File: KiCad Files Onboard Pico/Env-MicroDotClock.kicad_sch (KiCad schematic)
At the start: 59 parts, among them IC1 IS31FL3730-QFLS2-TR, IC2 IS31FL3730-QFLS2-TR, IC3 IS31FL3730-QFLS2-TR, IC4 IS31FL3730-QFLS2-TR, J1 Conn_01x06_Pin, M1 Dip-14 Socket, M2 Dip-14 Socket, M3 Dip-14 Socket, M4 Dip-14 Socket, M5 Dip-14 Socket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

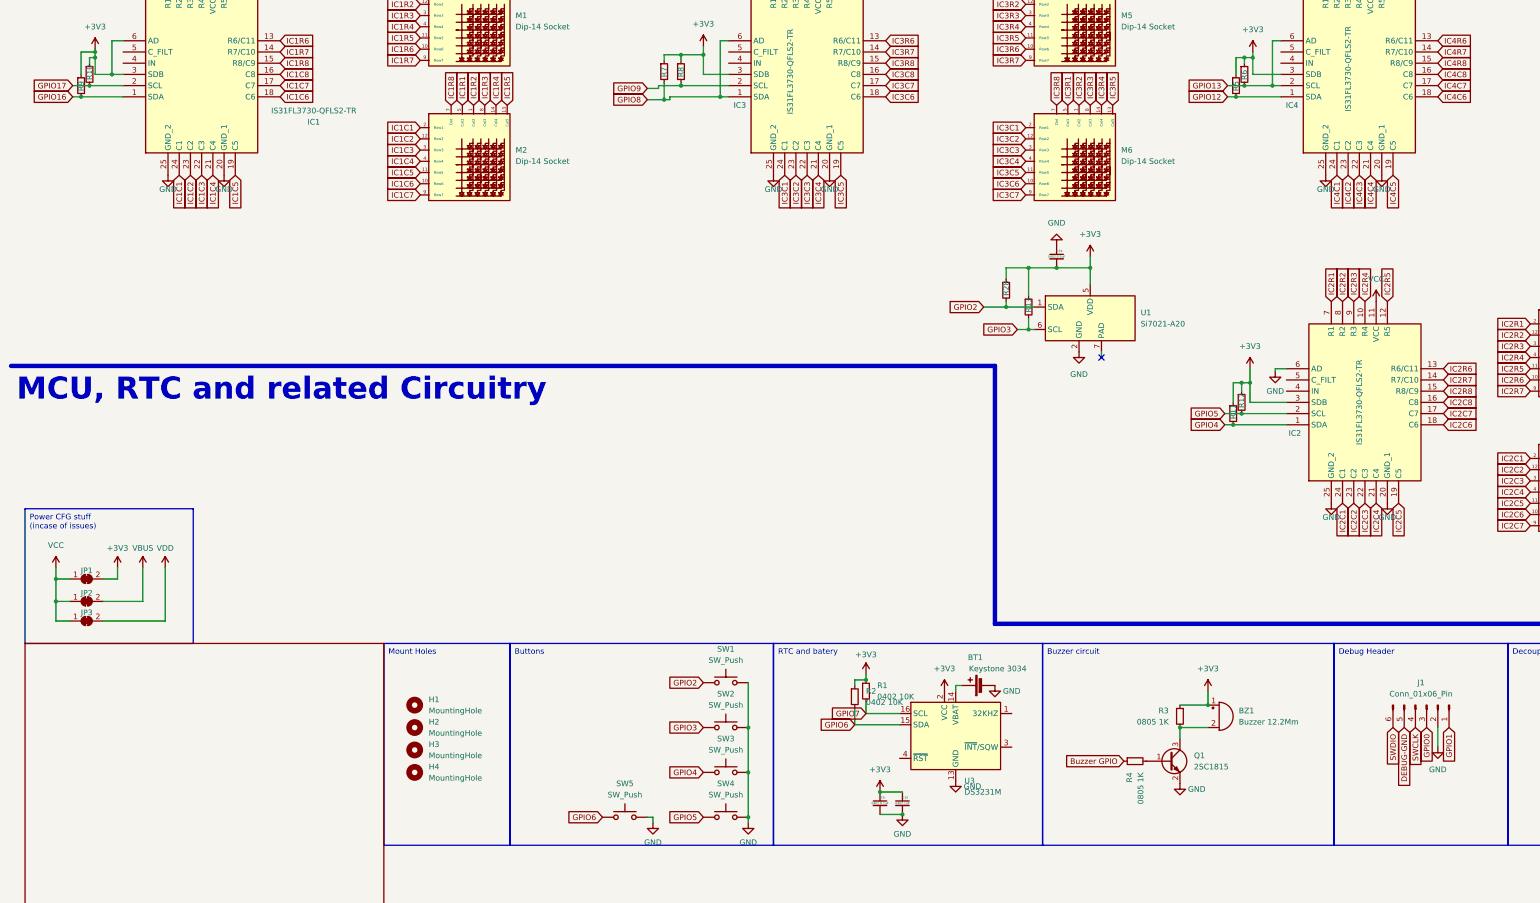
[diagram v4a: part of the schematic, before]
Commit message: began rework of onboard 2040 pcb
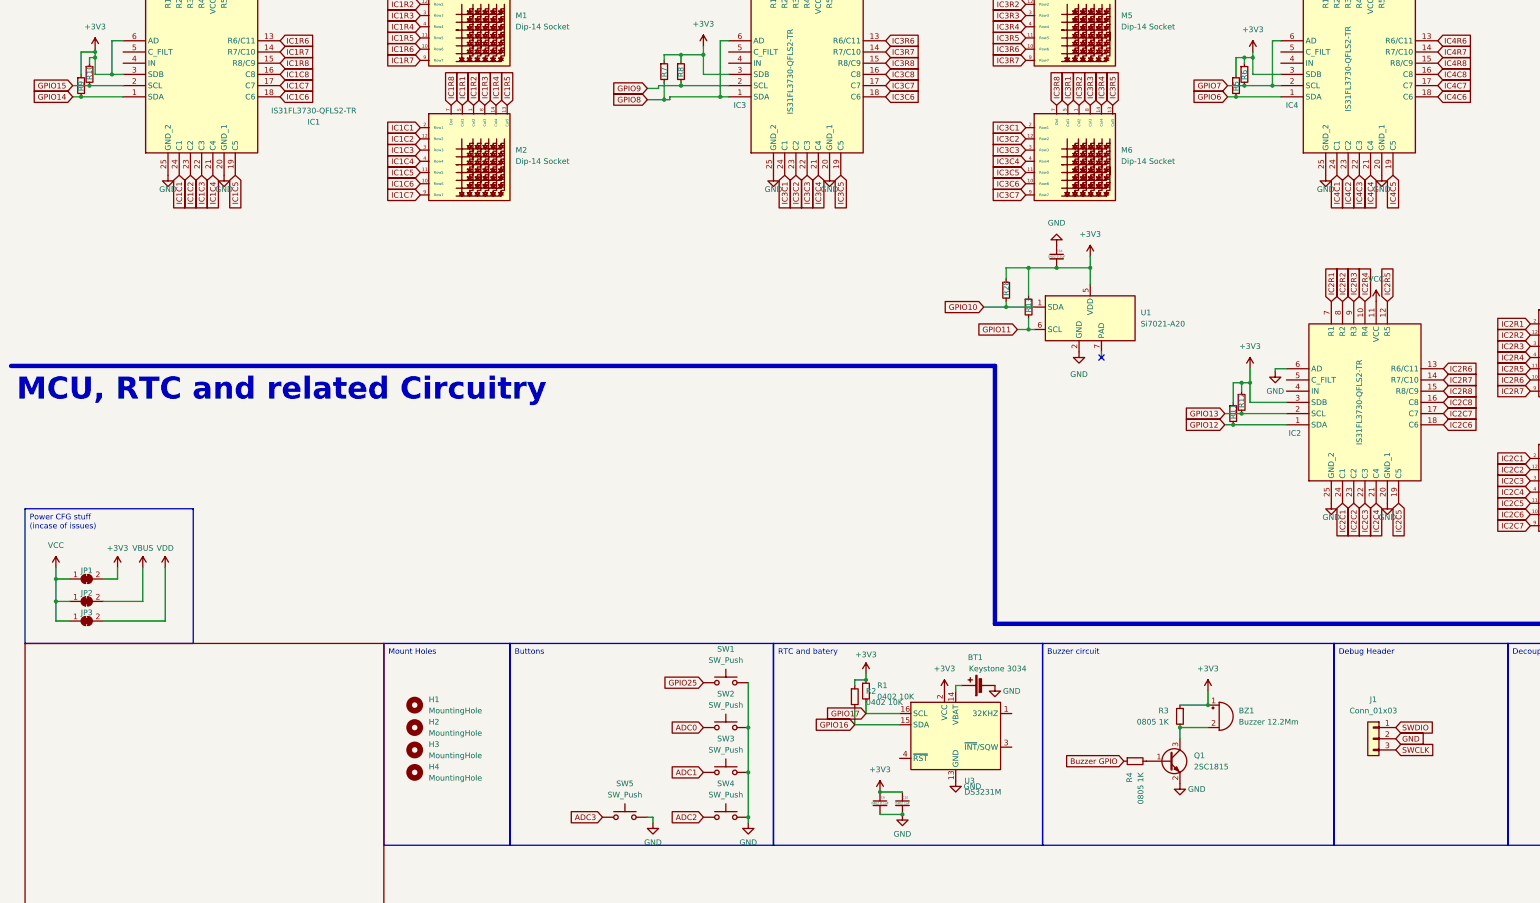
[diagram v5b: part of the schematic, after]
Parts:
- removed J1: Conn_01x06_Pin, Connector_PinHeader_2.54mm:PinHeader_1x06_P2.54mm_Vertical, symbol Connector:Conn_01x06_Pin
- added J1: Conn_01x03, Connector_PinHeader_1.00mm:PinHeader_1x03_P1.00mm_Vertical, symbol Connector_Generic:Conn_01x03
- R10, R11, R12, R13, R28, R5, R6, R7, R8, R9: value 0402 10K -> 0805 10K; footprint Resistor_SMD:R_0402_1005Metric -> Resistor_SMD:R_0805_2012Metric
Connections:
- net GND: now also J1.2 (Pin_2)
- net GPIO12: now also IC2.1 (SDA), R11.2; no longer IC4.1 (SDA), R5.2
- net GPIO13: now also IC2.2 (SCL), R12.2; no longer IC4.2 (SCL), IC4.6 (AD), R6.2
- net GPIO16: now also R2.2, U3.15 (SDA); no longer IC1.1 (SDA), R9.2
- net GPIO17: now also R1.2, U3.16 (SCL); no longer IC1.2 (SCL), R10.2
- net GPIO6: now also IC4.1 (SDA), R5.2; no longer R2.2, SW5.1, U3.15 (SDA)
- net GPIO7: now also IC4.2 (SCL), IC4.6 (AD), R6.2; no longer R1.2, U3.16 (SCL)
- net SWCLK: now also J1.3 (Pin_3)
- net SWDIO: now also J1.1 (Pin_1)
- net GPIO2 renamed GPIO10
- net GPIO10: no longer SW1.1
- net GPIO3 renamed GPIO11
- net GPIO11: no longer SW2.1
- removed net GPIO4: IC2.1 (SDA), R11.2, SW3.1
- removed net GPIO5: IC2.2 (SCL), R12.2, SW4.1
- new net ADC0: SW2.1
- new net ADC1: SW3.1
- new net ADC2: SW4.1
- new net ADC3: SW5.1
- new net GPIO14: IC1.1 (SDA), R9.2
- new net GPIO15: IC1.2 (SCL), R10.2
- new net GPIO25: SW1.1

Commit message: commit current progress
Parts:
- R10, R11, R12, R13, R28, R5, R6, R7, R8, R9: value 0805 10K -> 0402 10K; footprint Resistor_SMD:R_0805_2012Metric -> Resistor_SMD:R_0402_1005Metric
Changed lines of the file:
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@@
       (effects (font (size 1.27 1.27)) (justify left))
     )
-    (property "Value" "0805 10K" (at 162.56 73.66 0)
+    (property "Value" "0402 10K" (at 162.56 73.66 0)
       (effects (font (size 1.27 1.27)) (justify left) hide)
     )
-    (property "Footprint" "Resistor_SMD:R_0805_2012Metric" (at 160.02 72.39 0)
+    (property "Footprint" "Resistor_SMD:R_0402_1005Metric" (at 160.02 72.39 0)
       (effects (font (size 1.27 1.27)) hide)
     )
@@
       (effects (font (size 1.27 1.27)) (justify left))
     )
-    (property "Value" "0805 10K" (at 292.1 76.835 0)
+    (property "Value" "0402 10K" (at 292.1 76.835 0)
       (effects (font (size 1.27 1.27)) (justify left) hide)
     )
-    (property "Footprint" "Resistor_SMD:R_0805_2012Metric" (at 289.56 75.565 0)
+    (property "Footprint" "Resistor_SMD:R_0402_1005Metric" (at 289.56 75.565 0)
       (effects (font (size 1.27 1.27)) hide)
     )
@@
       (effects (font (size 1.27 1.27)) (justify left))
     )
-    (property "Value" "0805 10K" (at 240.03 123.19 0)
+    (property "Value" "0402 10K" (at 240.03 123.19 0)
       (effects (font (size 1.27 1.27)) (justify left) hide)
     )
-    (property "Footprint" "Resistor_SMD:R_0805_2012Metric" (at 237.49 121.92 0)
+    (property "Footprint" "Resistor_SMD:R_0402_1005Metric" (at 237.49 121.92 0)
       (effects (font (size 1.27 1.27)) hide)
     )
@@
       (effects (font (size 1.27 1.27)) (justify left))
     )
-    (property "Value" "0805 10K" (at 245.11 127 0)
+    (property "Value" "0402 10K" (at 245.11 127 0)
       (effects (font (size 1.27 1.27)) (justify left) hide)
     )
-    (property "Footprint" "Resistor_SMD:R_0805_2012Metric" (at 242.57 125.73 0)
+    (property "Footprint" "Resistor_SMD:R_0402_1005Metric" (at 242.57 125.73 0)
       (effects (font (size 1.27 1.27)) hide)
     )
@@
       (effects (font (size 1.27 1.27)) (justify left))
     )
-    (property "Value" "0805 10K" (at 166.37 73.66 0)
+    (property "Value" "0402 10K" (at 166.37 73.66 0)
       (effects (font (size 1.27 1.27)) (justify left) hide)
     )
-    (property "Footprint" "Resistor_SMD:R_0805_2012Metric" (at 163.83 72.39 0)
+    (property "Footprint" "Resistor_SMD:R_0402_1005Metric" (at 163.83 72.39 0)
       (effects (font (size 1.27 1.27)) hide)
     )
@@
       (effects (font (size 1.27 1.27)) (justify left))
     )
-    (property "Value" "0805 10K" (at 293.37 148.59 0)
+    (property "Value" "0402 10K" (at 293.37 148.59 0)
       (effects (font (size 1.27 1.27)) (justify left) hide)
     )
-    (property "Footprint" "Resistor_SMD:R_0805_2012Metric" (at 290.83 147.32 0)
+    (property "Footprint" "Resistor_SMD:R_0402_1005Metric" (at 290.83 147.32 0)
       (effects (font (size 1.27 1.27)) hide)
     )
@@
       (effects (font (size 1.27 1.27)) (justify left))
     )
-    (property "Value" "0805 10K" (at 294.005 74.295 0)
+    (property "Value" "0402 10K" (at 294.005 74.295 0)
       (effects (font (size 1.27 1.27)) (justify left) hide)
     )
-    (property "Footprint" "Resistor_SMD:R_0805_2012Metric" (at 291.465 73.025 0)
+    (property "Footprint" "Resistor_SMD:R_0402_1005Metric" (at 291.465 73.025 0)
       (effects (font (size 1.27 1.27)) hide)
     )
@@
       (effects (font (size 1.27 1.27)) (justify left))
     )
-    (property "Value" "0805 10K" (at 32.385 74.295 0)
+    (property "Value" "0402 10K" (at 32.385 74.295 0)
       (effects (font (size 1.27 1.27)) (justify left) hide)
     )
-    (property "Footprint" "Resistor_SMD:R_0805_2012Metric" (at 29.845 73.025 0)
+    (property "Footprint" "Resistor_SMD:R_0402_1005Metric" (at 29.845 73.025 0)
       (effects (font (size 1.27 1.27)) hide)
     )
@@
       (effects (font (size 1.27 1.27)) (justify left))
     )
-    (property "Value" "0805 10K" (at 291.465 151.13 0)
+    (property "Value" "0402 10K" (at 291.465 151.13 0)
       (effects (font (size 1.27 1.27)) (justify left) hide)
     )
-    (property "Footprint" "Resistor_SMD:R_0805_2012Metric" (at 288.925 149.86 0)
+    (property "Footprint" "Resistor_SMD:R_0402_1005Metric" (at 288.925 149.86 0)
       (effects (font (size 1.27 1.27)) hide)
     )
@@
       (effects (font (size 1.27 1.27)) (justify left))
     )
-    (property "Value" "0805 10K" (at 30.48 76.835 0)
+    (property "Value" "0402 10K" (at 30.48 76.835 0)
       (effects (font (size 1.27 1.27)) (justify left) hide)
     )
-    (property "Footprint" "Resistor_SMD:R_0805_2012Metric" (at 27.94 75.565 0)
-      (effects (font (size 1.27 1.27)) hide)
-    )
+    (property "Footprint" "Resistor_SMD:R_0402_1005Metric" (at 27.94 75.565 0)
+      (effects (font (size 1.27 1.27)) hide)
+    )

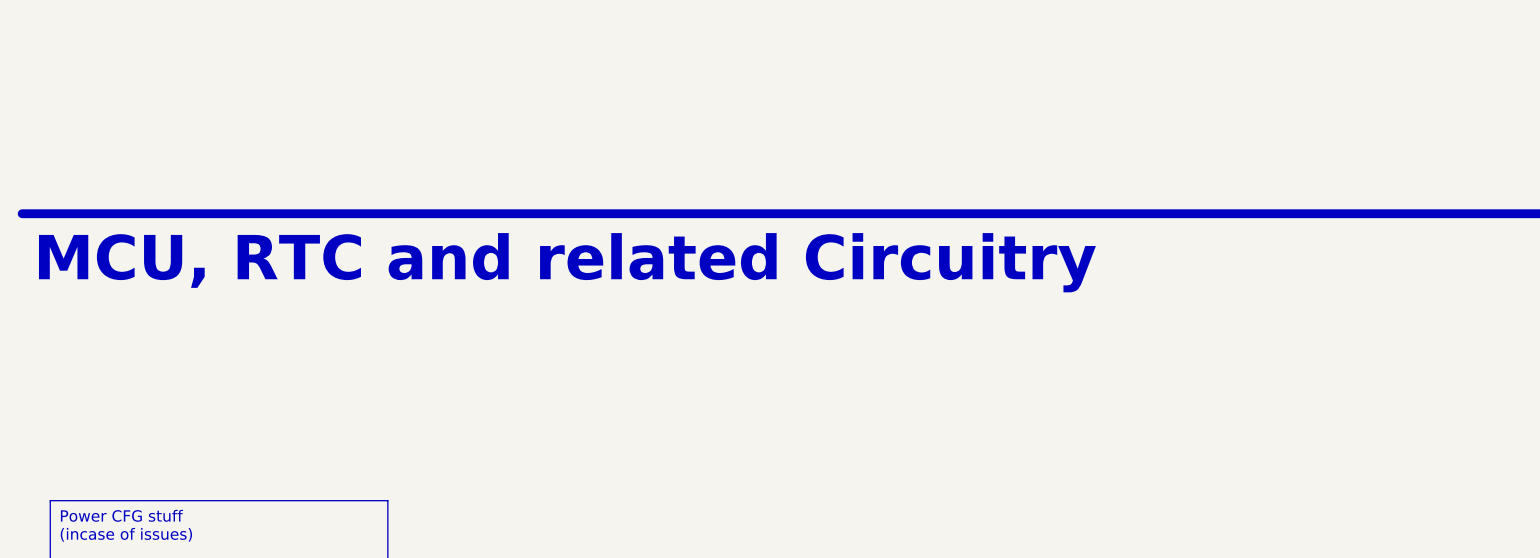
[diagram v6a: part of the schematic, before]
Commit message: finished up and cleaned up PCB, added logos
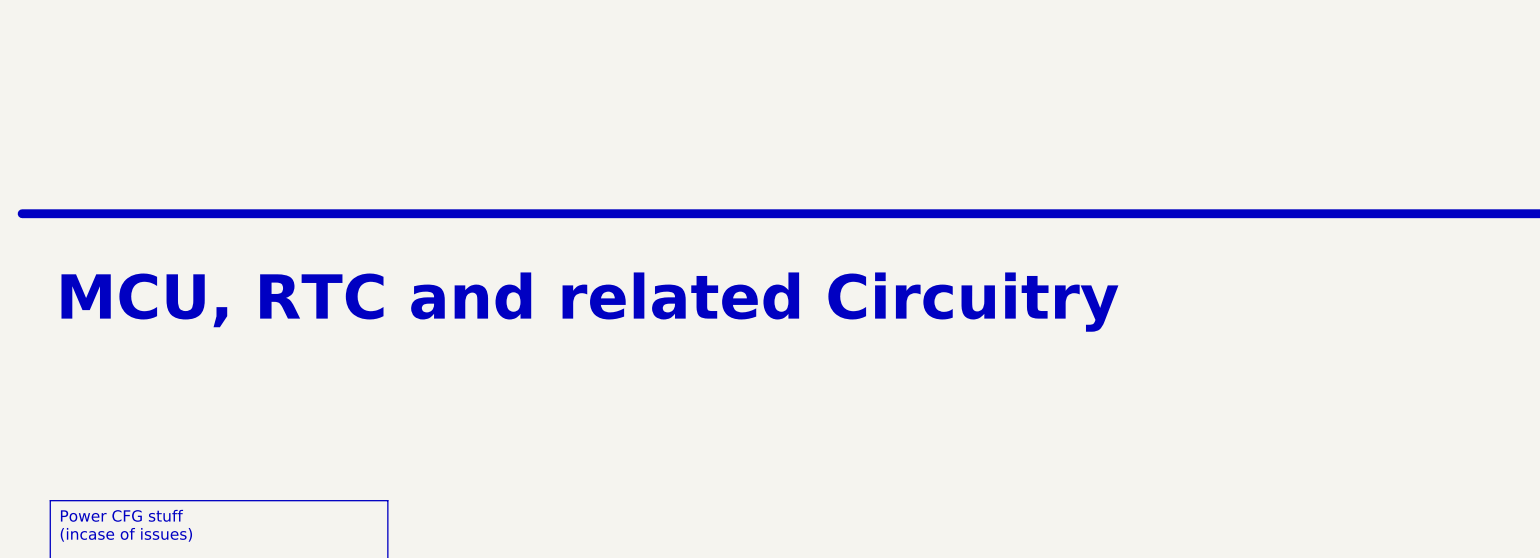
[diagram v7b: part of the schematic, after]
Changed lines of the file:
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@@
     (effects (font (size 5 5) (thickness 1) bold) (justify left bottom))
   )
-  (text "MCU, RTC and related Circuitry" (at 13.335 147.32 0)
+  (text "MCU, RTC and related Circuitry" (at 15.875 151.765 0)
     (effects (font (size 5 5) (thickness 1) bold) (justify left bottom))
   )

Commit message: generated production files
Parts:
- H1, H2, H3, H4: value MountingHole -> M2
- J1: value Conn_01x03 -> 1mm 1x3
- SW1, SW2, SW3, SW4, SW5: value SW_Push -> MX Keyboard Switch
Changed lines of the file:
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@@
       (effects (font (size 1.27 1.27)))
     )
-    (property "Value" "SW_Push" (at 173.99 226.06 0)
+    (property "Value" "MX Keyboard Switch" (at 173.99 226.06 0)
       (effects (font (size 1.27 1.27)))
     )
@@
       (effects (font (size 1.27 1.27)))
     )
-    (property "Value" "SW_Push" (at 151.13 236.22 0)
+    (property "Value" "MX Keyboard Switch" (at 151.13 236.22 0)
       (effects (font (size 1.27 1.27)))
     )
@@
       (effects (font (size 1.27 1.27)))
     )
-    (property "Value" "SW_Push" (at 173.99 236.22 0)
+    (property "Value" "MX Keyboard Switch" (at 173.99 236.22 0)
       (effects (font (size 1.27 1.27)))
     )
@@
       (effects (font (size 1.27 1.27)) (justify left))
     )
-    (property "Value" "MountingHole" (at 106.68 217.17 0)
+    (property "Value" "M2" (at 106.68 217.17 0)
       (effects (font (size 1.27 1.27)) (justify left))
     )
@@
       (effects (font (size 1.27 1.27)) (justify left))
     )
-    (property "Value" "MountingHole" (at 106.68 232.41 0)
+    (property "Value" "M2" (at 106.68 232.41 0)
       (effects (font (size 1.27 1.27)) (justify left))
     )
@@
       (effects (font (size 1.27 1.27)))
     )
-    (property "Value" "Conn_01x03" (at 320.675 217.17 0)
+    (property "Value" "1mm 1x3" (at 320.675 217.17 0)
       (effects (font (size 1.27 1.27)))
     )
@@
       (effects (font (size 1.27 1.27)) (justify left))
     )
-    (property "Value" "MountingHole" (at 106.68 227.33 0)
+    (property "Value" "M2" (at 106.68 227.33 0)
       (effects (font (size 1.27 1.27)) (justify left))
     )
@@
       (effects (font (size 1.27 1.27)))
     )
-    (property "Value" "SW_Push" (at 173.99 205.74 0)
+    (property "Value" "MX Keyboard Switch" (at 173.99 205.74 0)
       (effects (font (size 1.27 1.27)))
     )
@@
       (effects (font (size 1.27 1.27)) (justify left))
     )
-    (property "Value" "MountingHole" (at 106.68 222.25 0)
+    (property "Value" "M2" (at 106.68 222.25 0)
       (effects (font (size 1.27 1.27)) (justify left))
     )
@@
       (effects (font (size 1.27 1.27)))
     )
-    (property "Value" "SW_Push" (at 173.99 215.9 0)
-      (effects (font (size 1.27 1.27)))
-    )
+    (property "Value" "MX Keyboard Switch" (at 173.99 215.9 0)
+      (effects (font (size 1.27 1.27)))
+    )
